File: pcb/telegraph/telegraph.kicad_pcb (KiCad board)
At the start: 2 copper layers, 48 x 38 mm, 56 parts, among them J1 Conn_02x02_Counter_Clockwise, J2 Conn_01x02, Q1 RU1E002SPTCL, SW1 SW_SPST, U1 MSP430FR2512IRHLR, U2 RN42, U3 AP3513E, Y1 32.768kHz

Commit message: Finish PCB board
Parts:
- added C16: 1nF, Capacitors_SMD:C_0603_HandSoldering, B.Cu at (132.2, 128.1)
- added C17: 1uF, Capacitors_SMD:C_0805_HandSoldering, F.Cu at (119.9, 113.4)
- added R18: 100k, Resistors_SMD:R_0402, F.Cu at (133.0, 127.9)
- added R19: 100k, Resistors_SMD:R_0402, F.Cu at (133.0, 126.9)
- moved D1 2.61 mm to (126.2, 107.6)
- moved D2 2.61 mm to (124.5, 107.5)
- moved R2 1.30 mm to (121.6, 106.8)
- moved R3 1.30 mm to (121.5, 108.5)
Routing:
- net Net-(C17-Pad1): track 0.00 -> 5.93 mm, vias 0 -> 2
- net /SWBTDIO: track 21.3 -> 25.9 mm, vias 2 -> 3
- net /+3V3: track 97.3 -> 101.2 mm
- net GND: track 217.7 -> 221.1 mm
- net /RN42_CTS: track 19.2 -> 16.2 mm
- net Net-(R6-Pad2): track 8.17 -> 9.66 mm
- net Net-(D1-Pad1): track 4.32 -> 5.80 mm
- net Net-(R5-Pad1): track 7.89 -> 9.35 mm
- net Net-(R2-Pad2): track 2.85 -> 3.77 mm
- net Net-(D2-Pad1): track 2.40 -> 3.25 mm
- net Net-(R3-Pad2): track 3.69 -> 4.30 mm

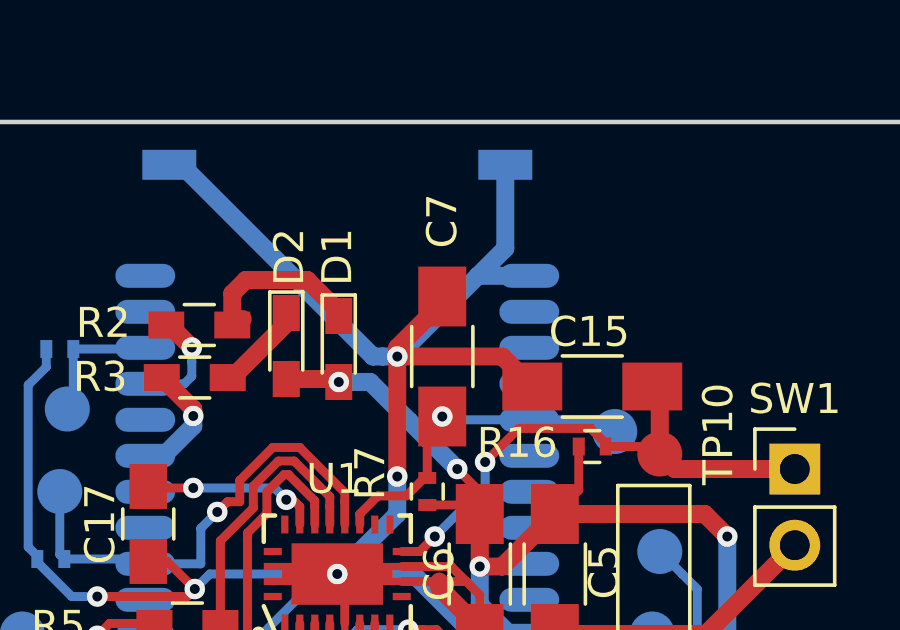
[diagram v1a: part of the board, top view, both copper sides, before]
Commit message: Replace RN42 RC pair with one easier to drive from MCU
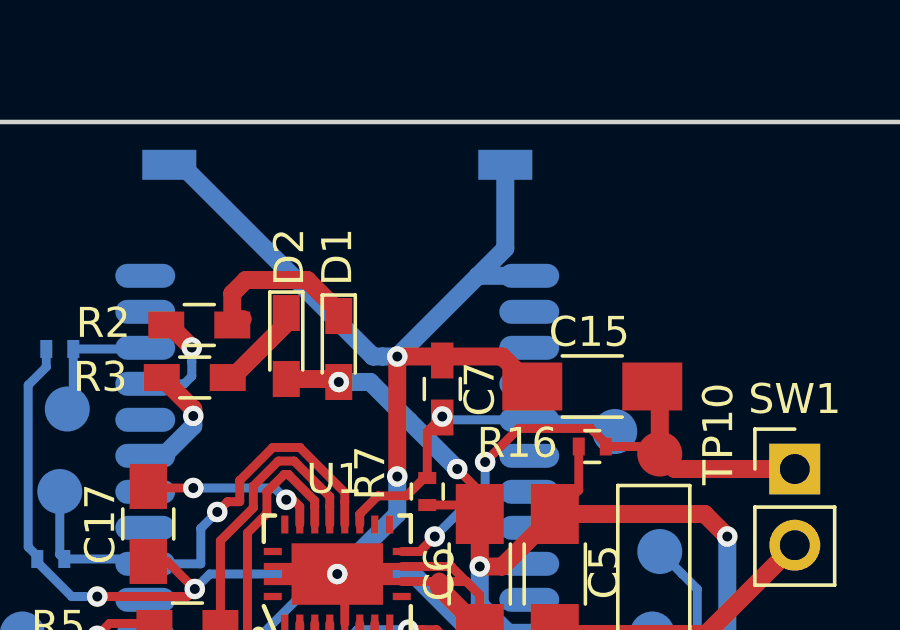
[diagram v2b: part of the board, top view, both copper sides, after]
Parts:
- C7: value 100nF -> 10nF; footprint Capacitors_SMD:C_1206_HandSoldering -> Capacitors_SMD:C_0603_HandSoldering
- R7: value 10k -> 100k
- moved C7 1.08 mm to (129.7, 108.9), turned to 270 degrees
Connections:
- C7 pad 1: /RN42_RSTN -> GND
- C7 pad 2: GND -> /RN42_RSTN
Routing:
- net GND: track 221.1 -> 218.5 mm
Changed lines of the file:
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@@
     (thickness 1.6)
     (drawings 4)
-    (tracks 452)
+    (tracks 449)
     (zones 0)
     (modules 60)
@@
     (add_net "Net-(U2-Pad9)")
   )
+  (module Capacitors_SMD:C_0603_HandSoldering (layer F.Cu)
+    (at 129.7 108.9 270)
+    (descr "Capacitor SMD 0603, hand soldering")
+    (tags "capacitor 0603")
+    (attr smd)
+    (fp_text reference C7 (at 0 -1.25 270) (layer F.SilkS)
+      (effects (font (size 1 1) (thickness 0.15)))
+    )
+    (fp_text value 10nF (at 0 1.5 270) (layer F.Fab)
+      (effects (font (size 1 1) (thickness 0.15)))
+    )
+    (fp_line (start 1.8 0.65) (end -1.8 0.65) (layer F.CrtYd) (width 0.05))
+    (fp_line (start 1.8 0.65) (end 1.8 -0.65) (layer F.CrtYd) (width 0.05))
+    (fp_line (start -1.8 -0.65) (end -1.8 0.65) (layer F.CrtYd) (width 0.05))
+    (fp_line (start -1.8 -0.65) (end 1.8 -0.65) (layer F.CrtYd) (width 0.05))
+    (fp_line (start 0.35 0.6) (end -0.35 0.6) (layer F.SilkS) (width 0.12))
+    (fp_line (start -0.35 -0.6) (end 0.35 -0.6) (layer F.SilkS) (width 0.12))
+    (fp_line (start -0.8 -0.4) (end 0.8 -0.4) (layer F.Fab) (width 0.1))
+    (fp_line (start 0.8 -0.4) (end 0.8 0.4) (layer F.Fab) (width 0.1))
+    (fp_line (start 0.8 0.4) (end -0.8 0.4) (layer F.Fab) (width 0.1))
+    (fp_line (start -0.8 0.4) (end -0.8 -0.4) (layer F.Fab) (width 0.1))
+    (fp_text user %R (at 0 -1.25 270) (layer F.Fab)
+      (effects (font (size 1 1) (thickness 0.15)))
+    )
+    (pad 2 smd rect (at 0.95 0 270) (size 1.2 0.75) (layers F.Cu F.Paste F.Mask)
+      (net 13 /RN42_RSTN))
+    (pad 1 smd rect (at -0.95 0 270) (size 1.2 0.75) (layers F.Cu F.Paste F.Mask)
+      (net 5 GND))
+    (model Capacitors_SMD.3dshapes/C_0603.wrl
+      (at (xyz 0 0 0))
+      (scale (xyz 1 1 1))
+      (rotate (xyz 0 0 0))
+    )
+  )
   (module Capacitors_SMD:C_0805_HandSoldering (layer F.Cu)
     (at 119.9 113.4 270)
@@
       (net 21 /+VBAT))
     (pad 1 smd rect (at -2 0) (size 2 1.6) (layers B.Cu B.Paste B.Mask)
-      (net 5 GND))
-    (model Capacitors_SMD.3dshapes/C_1206.wrl
-      (at (xyz 0 0 0))
-      (scale (xyz 1 1 1))
-      (rotate (xyz 0 0 0))
-    )
-  )
-  (module Capacitors_SMD:C_1206_HandSoldering (layer F.Cu)
-    (at 129.7 107.818 90)
-    (descr "Capacitor SMD 1206, hand soldering")
-    (tags "capacitor 1206")
-    (attr smd)
-    (fp_text reference C7 (at 4.518 0 90) (layer F.SilkS)
-      (effects (font (size 1 1) (thickness 0.15)))
-    )
-    (fp_text value 100nF (at 0 2 90) (layer F.Fab)
-      (effects (font (size 1 1) (thickness 0.15)))
-    )
-    (fp_text user %R (at 0 -1.75 90) (layer F.Fab)
-      (effects (font (size 1 1) (thickness 0.15)))
-    )
-    (fp_line (start -1.6 0.8) (end -1.6 -0.8) (layer F.Fab) (width 0.1))
-    (fp_line (start 1.6 0.8) (end -1.6 0.8) (layer F.Fab) (width 0.1))
-    (fp_line (start 1.6 -0.8) (end 1.6 0.8) (layer F.Fab) (width 0.1))
-    (fp_line (start -1.6 -0.8) (end 1.6 -0.8) (layer F.Fab) (width 0.1))
-    (fp_line (start 1 -1.02) (end -1 -1.02) (layer F.SilkS) (width 0.12))
-    (fp_line (start -1 1.02) (end 1 1.02) (layer F.SilkS) (width 0.12))
-    (fp_line (start -3.25 -1.05) (end 3.25 -1.05) (layer F.CrtYd) (width 0.05))
-    (fp_line (start -3.25 -1.05) (end -3.25 1.05) (layer F.CrtYd) (width 0.05))
-    (fp_line (start 3.25 1.05) (end 3.25 -1.05) (layer F.CrtYd) (width 0.05))
-    (fp_line (start 3.25 1.05) (end -3.25 1.05) (layer F.CrtYd) (width 0.05))
-    (pad 1 smd rect (at -2 0 90) (size 2 1.6) (layers F.Cu F.Paste F.Mask)
-      (net 13 /RN42_RSTN))
-    (pad 2 smd rect (at 2 0 90) (size 2 1.6) (layers F.Cu F.Paste F.Mask)
       (net 5 GND))
     (model Capacitors_SMD.3dshapes/C_1206.wrl
@@
       (effects (font (size 1 1) (thickness 0.15)))
     )
-    (fp_text value 10k (at 0 1.45 90) (layer F.Fab)
+    (fp_text value 100k (at 0 1.45 90) (layer F.Fab)
       (effects (font (size 1 1) (thickness 0.15)))
     )
@@
   (segment (start 121.45 115.568) (end 121.95 115.068) (width 0.3) (layer B.Cu) (net 5))
   (via (at 128.2 111.818) (size 0.6858) (drill 0.3302) (layers F.Cu B.Cu) (net 5))
-  (segment (start 129.7 105.818) (end 129.7 106.018) (width 0.6) (layer F.Cu) (net 5))
-  (segment (start 129.7 106.018) (end 128.2 107.518) (width 0.6) (layer F.Cu) (net 5))
   (segment (start 128.2 113.068) (end 126.2 115.068) (width 0.6) (layer B.Cu) (net 5))
   (segment (start 128.2 111.818) (end 128.2 113.068) (width 0.6) (layer B.Cu) (net 5))
@@
   (segment (start 130.89 105.128) (end 128.2 107.818) (width 0.6) (layer B.Cu) (net 5))
   (segment (start 132.6 105.128) (end 130.89 105.128) (width 0.6) (layer B.Cu) (net 5))
-  (segment (start 128.2 107.518) (end 128.2 107.818) (width 0.6) (layer F.Cu) (net 5))
   (segment (start 128.2 107.818) (end 128.2 111.818) (width 0.6) (layer F.Cu) (net 5))
   (segment (start 131.7 107.818) (end 128.2 107.818) (width 0.6) (layer F.Cu) (net 5))
